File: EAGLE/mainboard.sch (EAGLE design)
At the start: 16 parts, among them IC1 7805TV

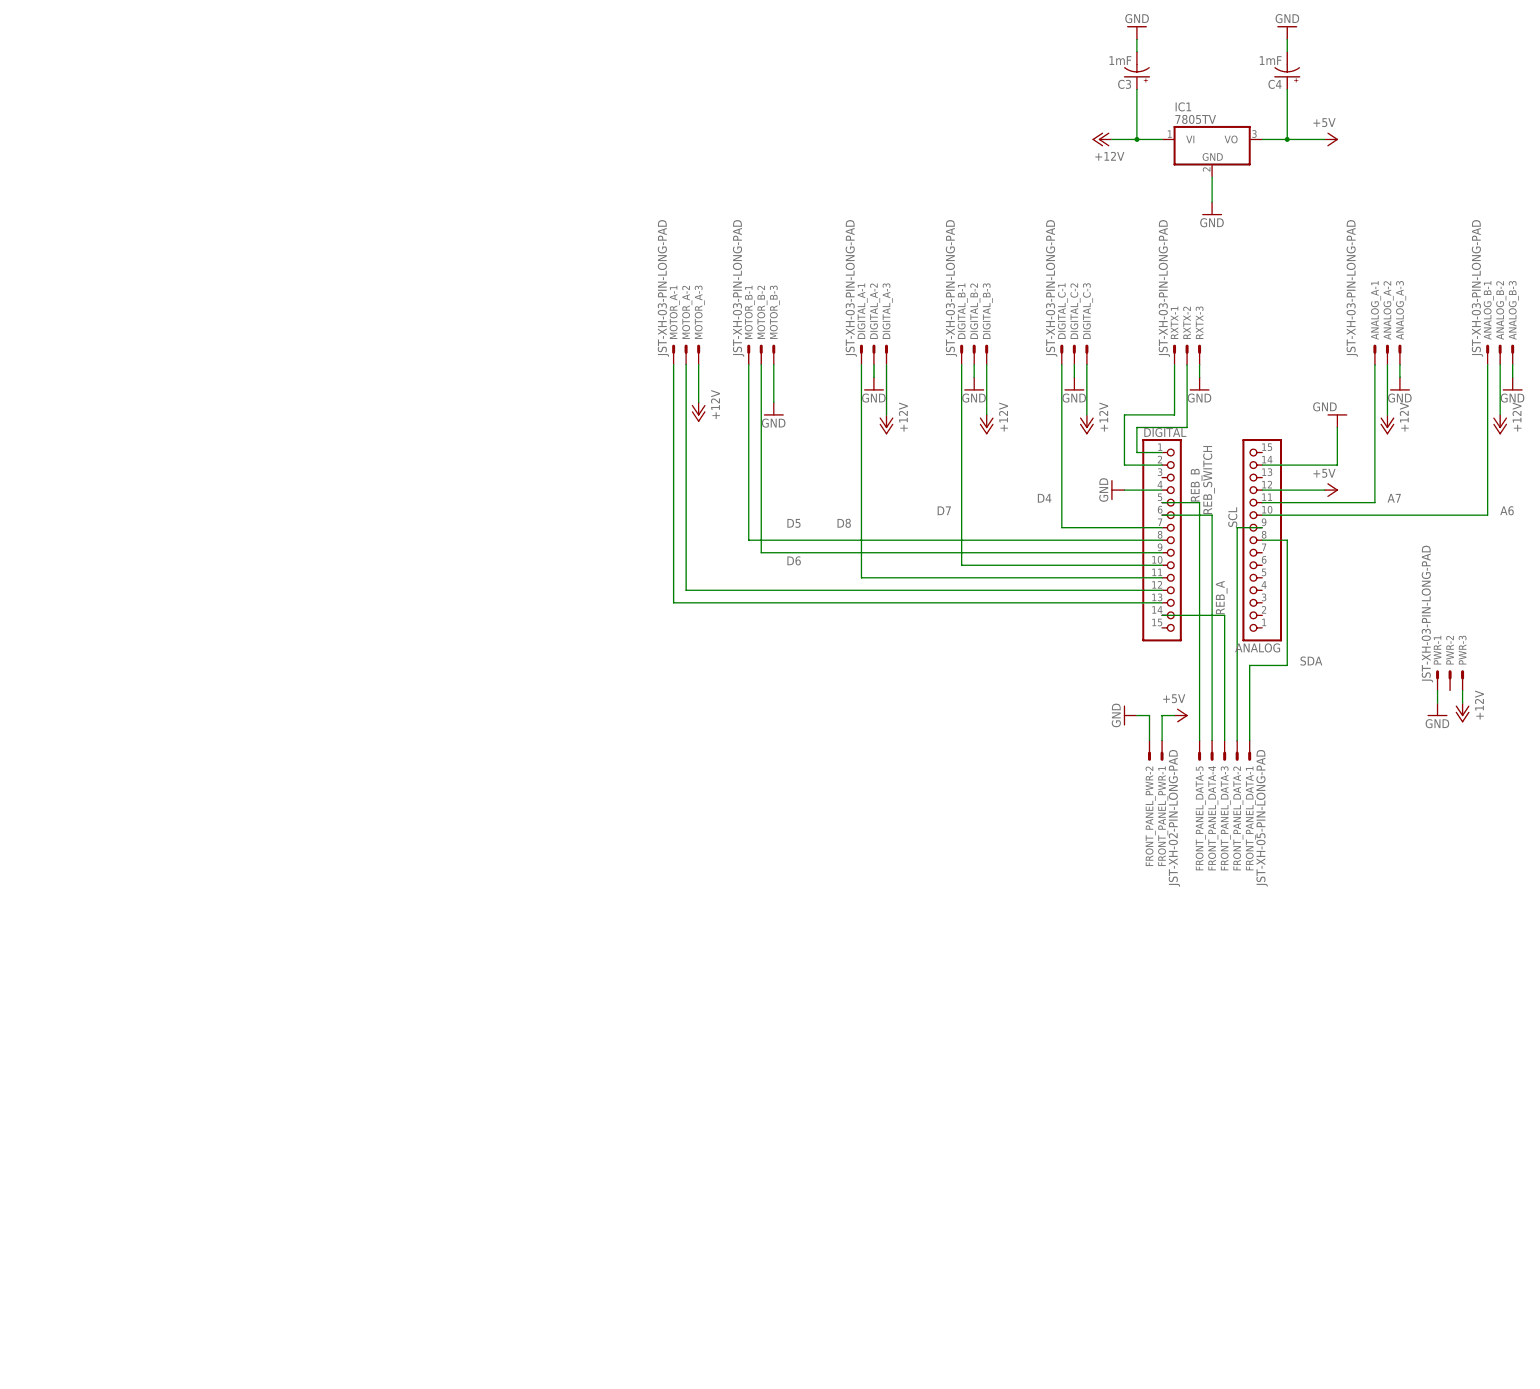
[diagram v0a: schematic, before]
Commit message: * Moved all EAGLE files into the project * Removed old copy-pasted boards * Updated .gitignore
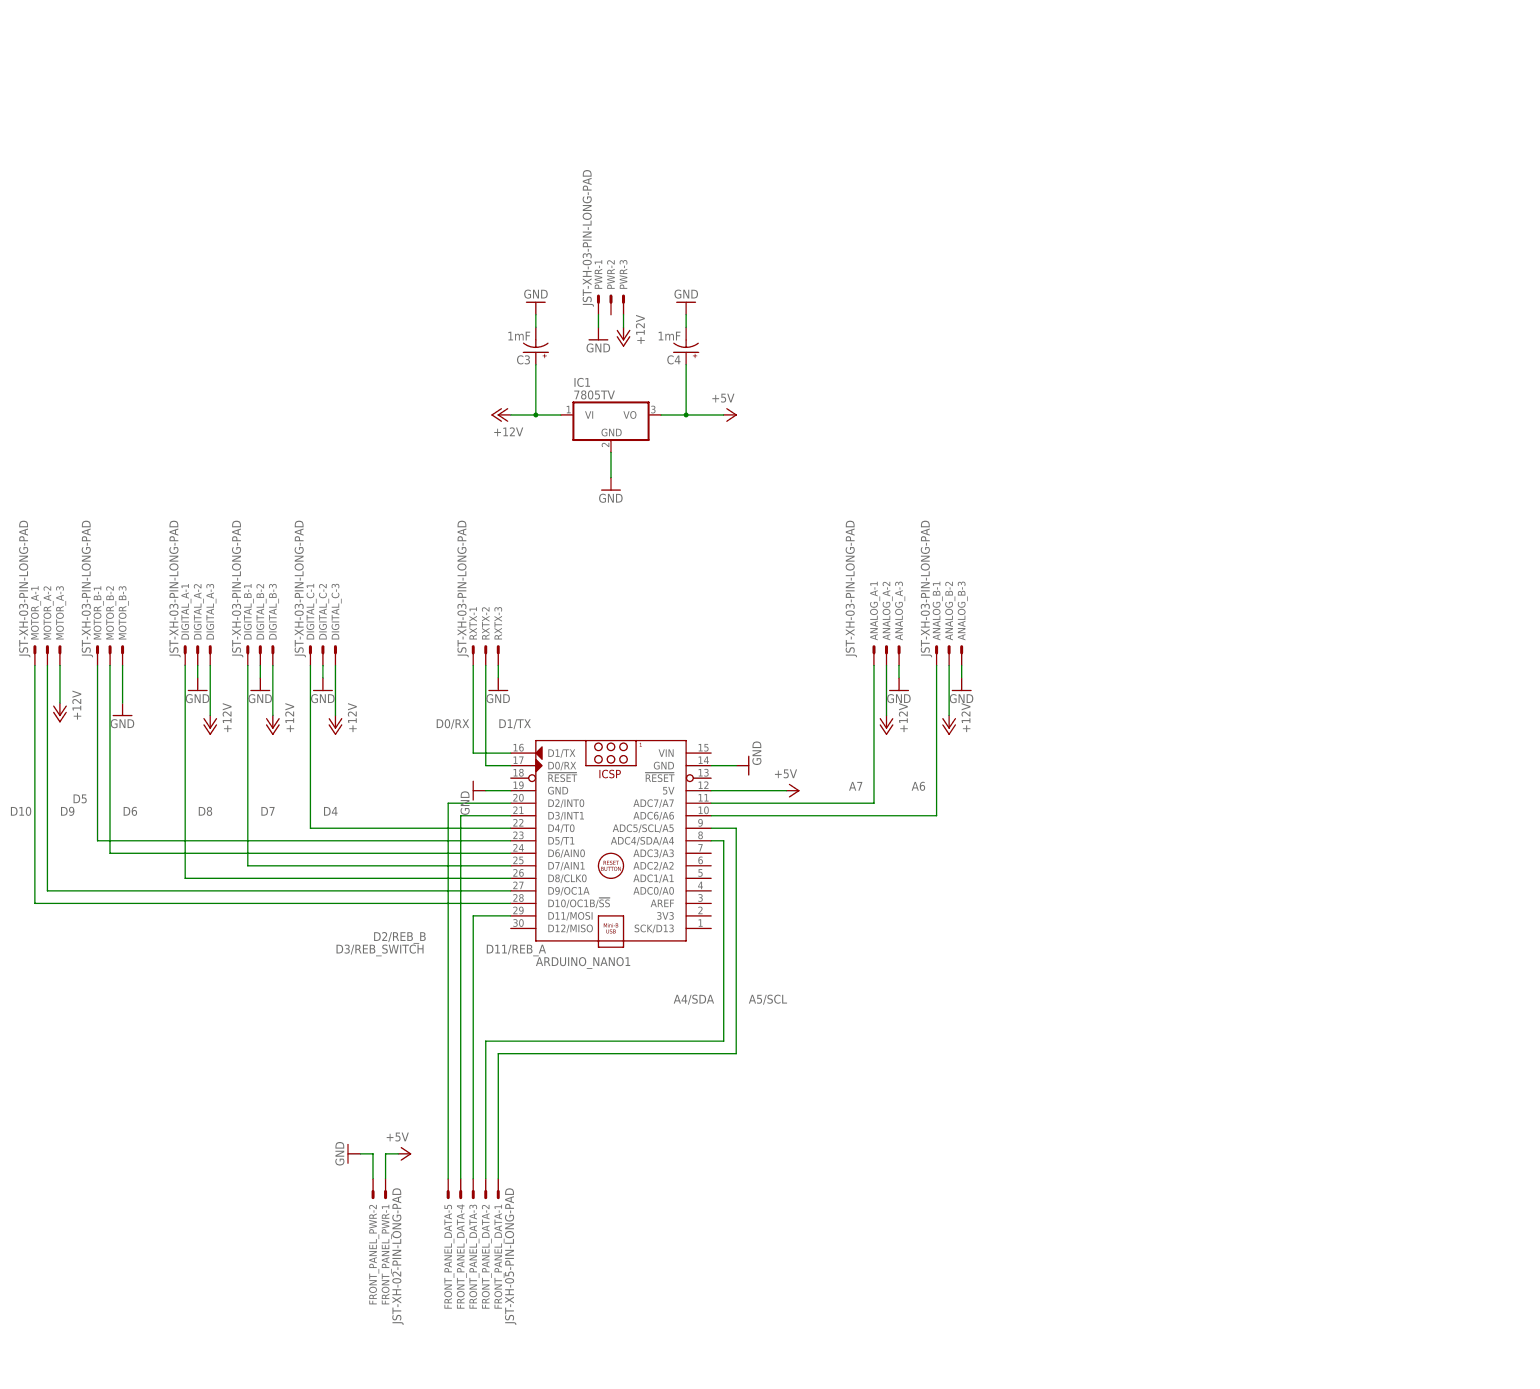
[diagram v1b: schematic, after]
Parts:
- removed ANALOG, DIGITAL: (no value), pinhead:PINHD-1X15
- added ARDUINO_NANO1: (no value), ArduinoNanoV30:ARDUINO_NANO
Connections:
- removed net REB_A: DIGITAL.14, FRONT_PANEL_DATA-3.S
- removed net REB_B: DIGITAL.5, FRONT_PANEL_DATA-5.S
- removed net REB_SWITCH: DIGITAL.6, FRONT_PANEL_DATA-4.S
- removed net RXD: DIGITAL.2, RXTX-1.S
- removed net SCL: ANALOG.9, FRONT_PANEL_DATA-2.S
- removed net SDA: ANALOG.8, FRONT_PANEL_DATA-1.S
- removed net TXD: DIGITAL.1, RXTX-2.S
- new net A4/SDA: ARDUINO_NANO1.ADC4/SDA/A4, FRONT_PANEL_DATA-2.S
- new net A5/SCL: ARDUINO_NANO1.ADC5/SCL/A5, FRONT_PANEL_DATA-1.S
- new net D0/RX: ARDUINO_NANO1.D0/RX, RXTX-2.S
- new net D1/TX: ARDUINO_NANO1.D1/TX, RXTX-1.S
- new net D11/REB_A: ARDUINO_NANO1.D11/MOSI, FRONT_PANEL_DATA-3.S
- new net D2/REB_B: ARDUINO_NANO1.D2/INT0, FRONT_PANEL_DATA-5.S
- new net D3/REB_SWITCH: ARDUINO_NANO1.D3/INT1, FRONT_PANEL_DATA-4.S
- net +5V: now also ARDUINO_NANO1.5V; no longer ANALOG.12
- net A6: now also ARDUINO_NANO1.ADC6/A6; no longer ANALOG.10
- net A7: now also ARDUINO_NANO1.ADC7/A7; no longer ANALOG.11
- net D10: now also ARDUINO_NANO1.D10/OC1B/!SS; no longer DIGITAL.13
- net D4: now also ARDUINO_NANO1.D4/T0; no longer DIGITAL.7
- net D5: now also ARDUINO_NANO1.D5/T1; no longer DIGITAL.8
- net D6: now also ARDUINO_NANO1.D6/AIN0; no longer DIGITAL.9
- net D7: now also ARDUINO_NANO1.D7/AIN1; no longer DIGITAL.10
- net D8: now also ARDUINO_NANO1.D8/CLK0; no longer DIGITAL.11
- net D9: now also ARDUINO_NANO1.D9/OC1A; no longer DIGITAL.12
- net GND: now also ARDUINO_NANO1.GND@1, ARDUINO_NANO1.GND@2; no longer ANALOG.14, DIGITAL.4
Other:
- moved on the sheet: ANALOG_A-1, ANALOG_A-2, ANALOG_A-3, ANALOG_B-1, ANALOG_B-2, ANALOG_B-3, C3, C4, DIGITAL_A-1, DIGITAL_A-2, DIGITAL_A-3, DIGITAL_B-1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
